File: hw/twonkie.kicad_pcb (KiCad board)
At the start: 4 copper layers, 25.4 x 25.4 mm, 58 parts, among them J1 USB4151, J2 690-024-294T331, J3 629105150521, Q1 BSD840N, Q2 BSD840N, Q3 BSD840N, SW1 EVQ-P7M01P, U1 INA260, U2 INA260, U3 MIC5504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

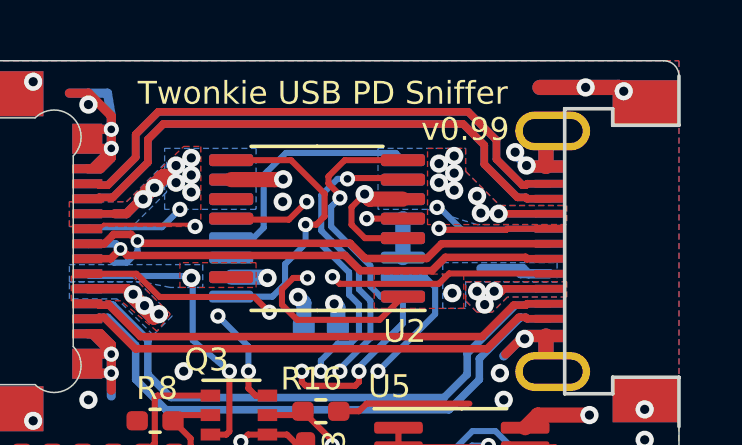
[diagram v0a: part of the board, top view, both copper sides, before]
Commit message: Bump silkscreen version to 1.0
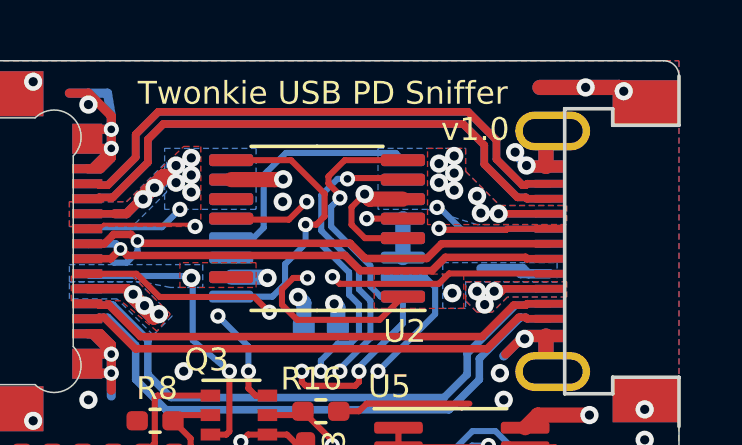
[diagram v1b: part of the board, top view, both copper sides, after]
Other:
- board text added: "v1.0"
- board text removed: "v0.99"
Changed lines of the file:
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@@
     (effects (font (size 0.6858 0.6858) (thickness 0.127)) (justify mirror))
   )
-  (gr_text v0.99 (at 91.6305 36.576) (layer F.SilkS)
+  (gr_text v1.0 (at 91.6305 36.576) (layer F.SilkS)
     (effects (font (size 0.762 0.762) (thickness 0.127)) (justify right))
   )

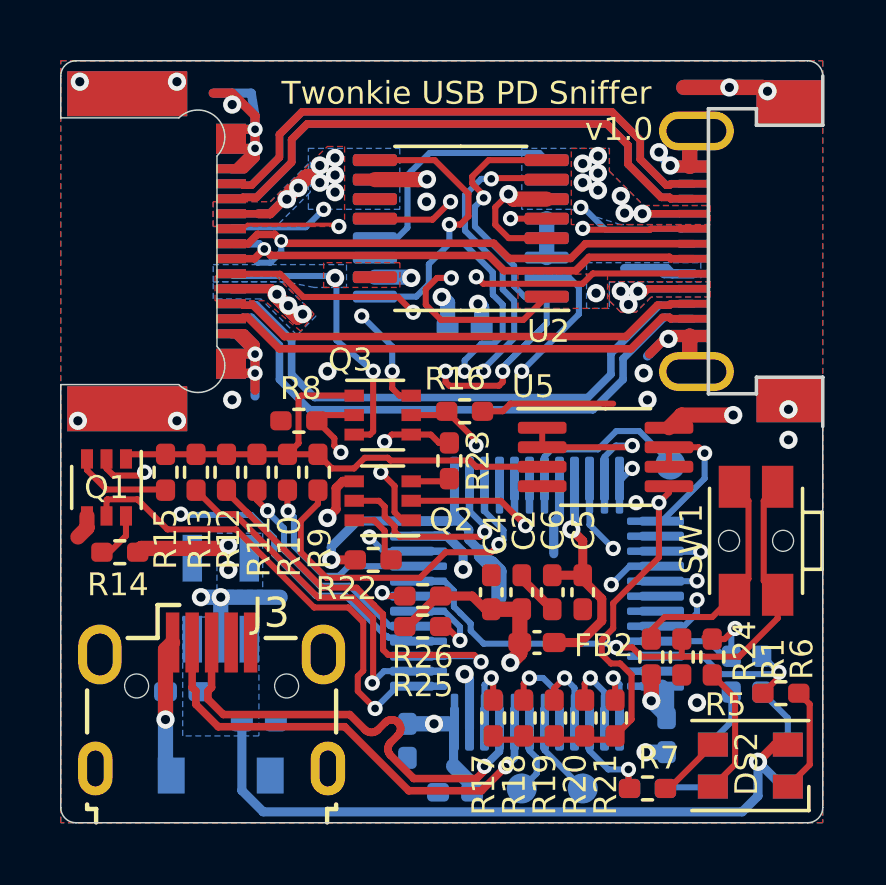
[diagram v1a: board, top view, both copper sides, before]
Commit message: Add back bootloader selection via USB_ID
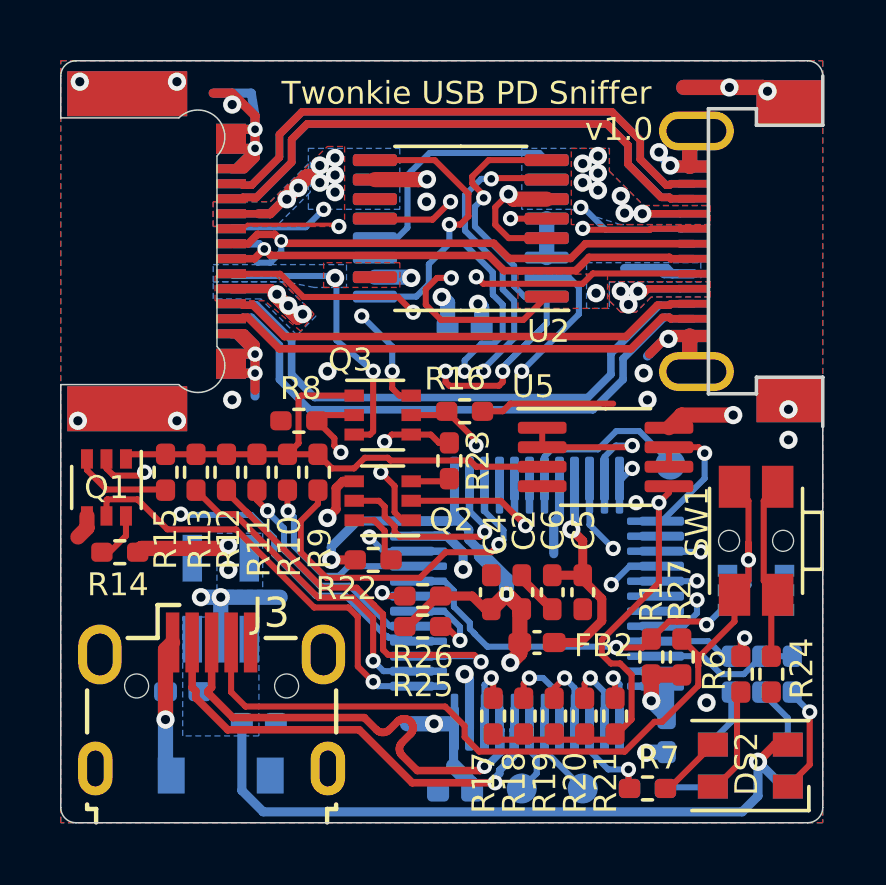
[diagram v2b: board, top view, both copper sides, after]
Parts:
- removed C8: 100n, Capacitor_SMD:C_0402_1005Metric_Pad0.74x0.62mm_HandSolder
- added Q4: BSD840N, Package_TO_SOT_SMD:SOT-363_SC-70-6, B.Cu at (95.1, 51.9)
- added R27: 35k7, Resistor_SMD:R_0402_1005Metric_Pad0.72x0.64mm_HandSolder, F.Cu at (92.6, 54.2)
- R5: moved to B.Cu
- moved R24 4.04 mm to (95.6, 54.7), turned to 270 degrees
- moved R6 1.11 mm to (94.6, 54.7)
- moved R1 1.02 mm to (91.6, 54.2), turned to 90 degrees
- moved R5 0.74 mm to (96.3, 54.7), turned to 90 degrees
- moved R17 0.06 mm to (86.3, 56.1)
- moved R18 0.06 mm to (87.3, 56.1)
- moved R19 0.06 mm to (88.3, 56.1)
- moved R20 0.06 mm to (89.3, 56.1)
- moved R21 0.06 mm to (90.4, 56.1)
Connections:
- J3 pad 4: Net-(J3-Pad4) -> /USB_B_ID
- R1 pad 1: /BOOT -> +3V3
- R1 pad 2: GND -> /BOOT
- R24 pad 1: +3V3 -> Net-(R24-Pad1)
- R24 pad 2: Net-(R24-Pad2) -> GND
- SW1 pad 1: Net-(R24-Pad2) -> /USB_B_ID
- SW1 pad 2: /BOOT -> Net-(R24-Pad1)
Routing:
- net /USB_B_ID: track 0.00 -> 30.1 mm, vias 0 -> 1
- net Net-(R24-Pad2): track 7.83 -> 0.00 mm
- net /BOOT: track 19.5 -> 12.5 mm, vias 1 -> 2
- net Net-(R24-Pad1): track 0.00 -> 6.12 mm
- net +3V3: track 45.0 -> 46.4 mm, vias 12 -> 13
- net /CC1_TX_EN: track 15.5 -> 14.3 mm
- net /LED_R_L: track 6.05 -> 4.84 mm, vias 1 -> 0
- net /CC1_RPUSB: track 11.5 -> 10.7 mm
- net Net-(DS2-Pad4): track 4.34 -> 3.60 mm
- net Net-(DS2-Pad1): track 3.57 -> 3.69 mm, vias 0 -> 1

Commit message: Improve U4 supply routing
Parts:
- moved C6 1.08 mm to (89.3, 52.0), turned to 90 degrees
- moved C5 0.95 mm to (88.3, 52.0), turned to 90 degrees
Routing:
- net GND: track 65.6 -> 64.0 mm, vias 30 -> 31
- net +3V3: track 46.4 -> 45.6 mm, vias 13 -> 12
- net /CC2_TX_DATA: track 9.77 -> 10.4 mm, vias 2 -> 1
